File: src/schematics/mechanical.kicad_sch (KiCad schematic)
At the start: 38 parts, among them U1 TPS565242DRDR, U2 TPS562202DRLR, U3 TPS562202DRLR, U4 TPS562202DRLR, U5 LM3880MF*-1AA

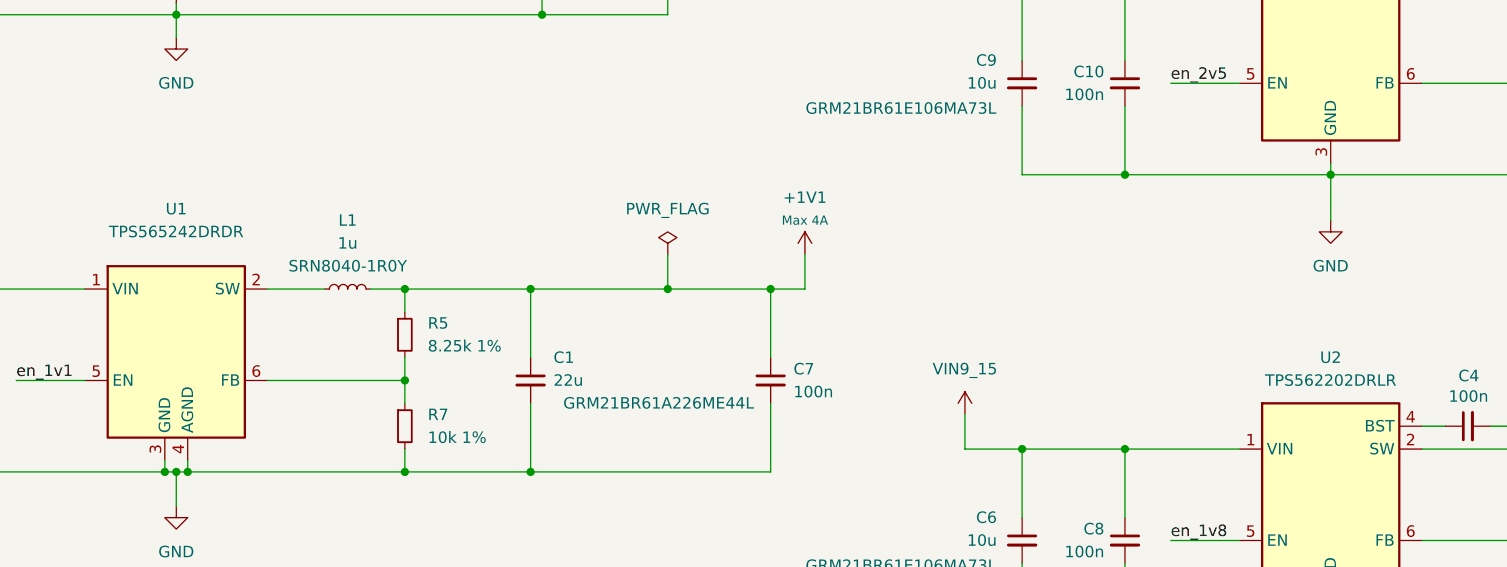
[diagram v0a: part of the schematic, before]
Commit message: Add length matching for DDR on L4 and L6. Todo L1 and redo L6
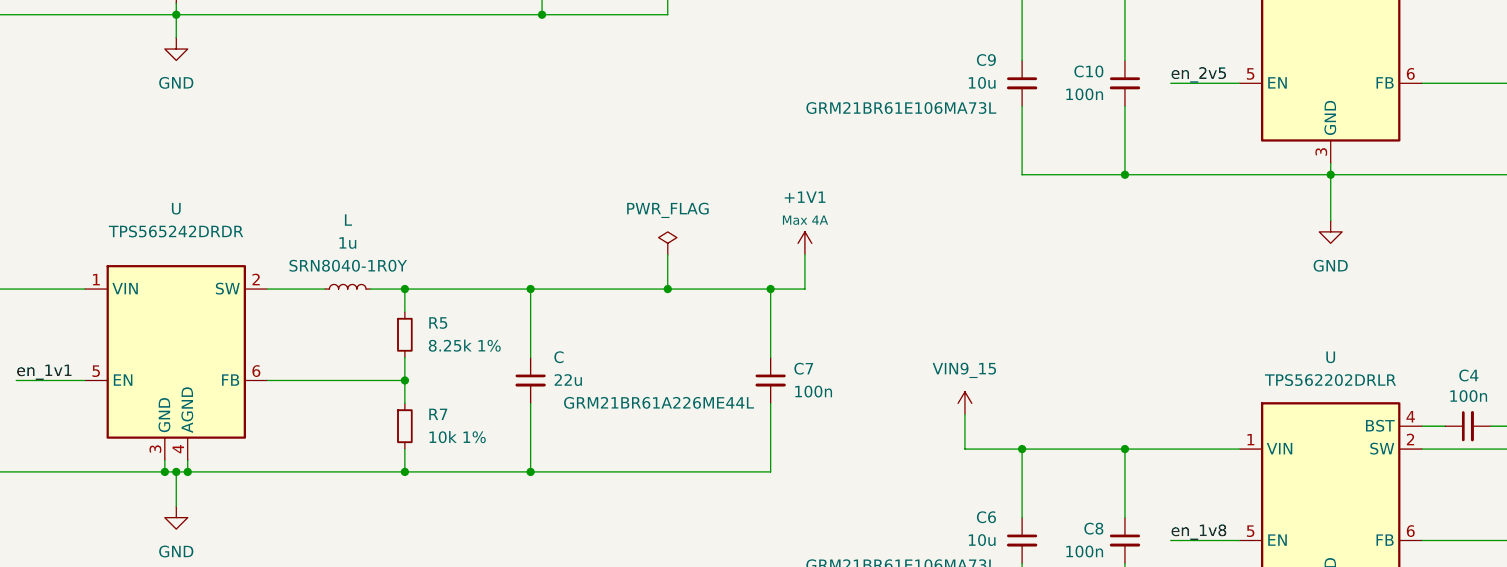
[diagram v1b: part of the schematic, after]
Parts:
- renumbered C1 to C, L1 to L, U2 to U, U1 to U

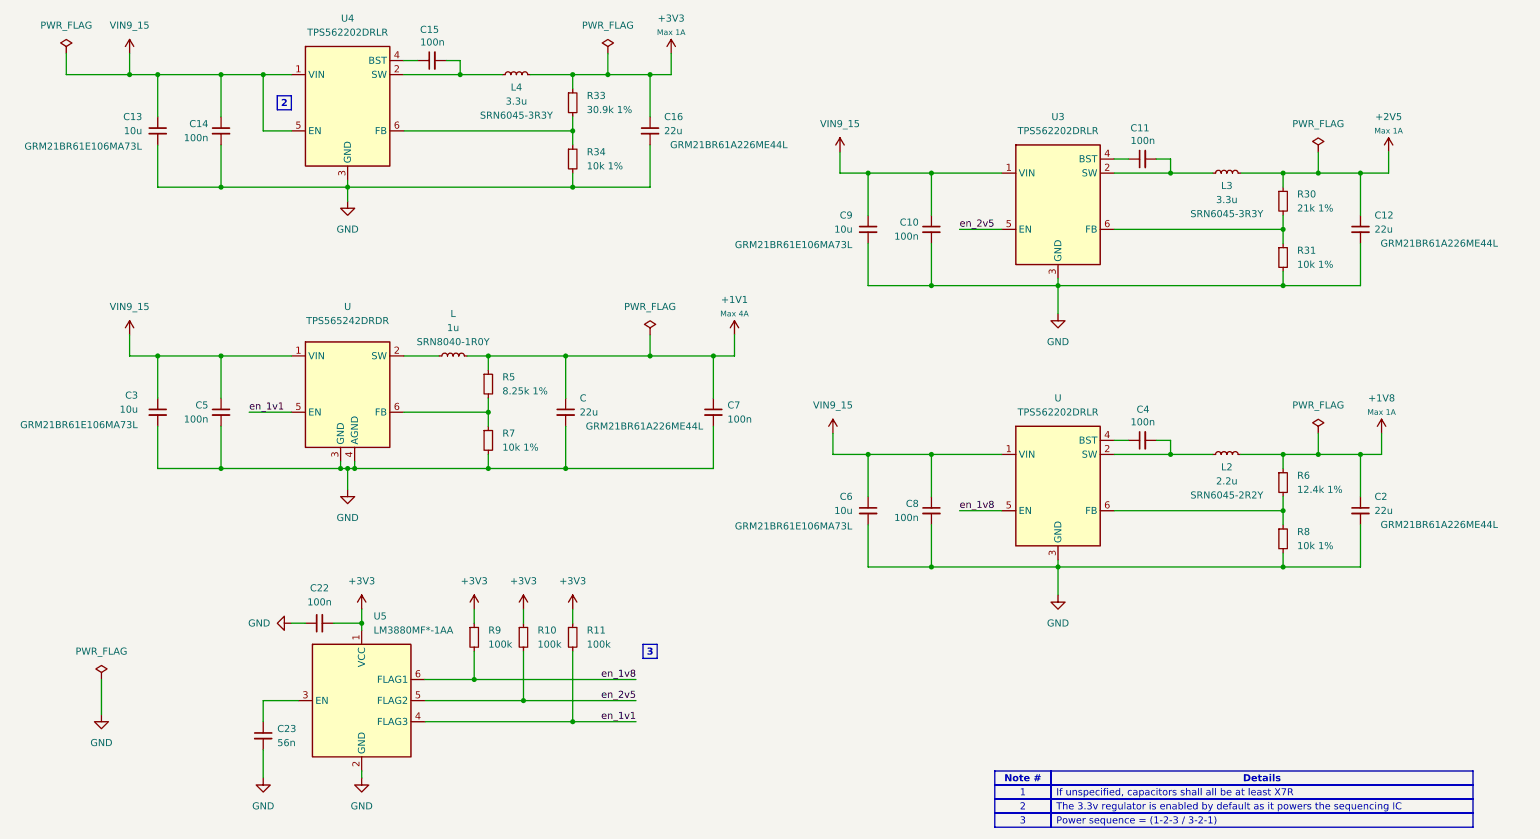
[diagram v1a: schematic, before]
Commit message: Fixed mechanical holes
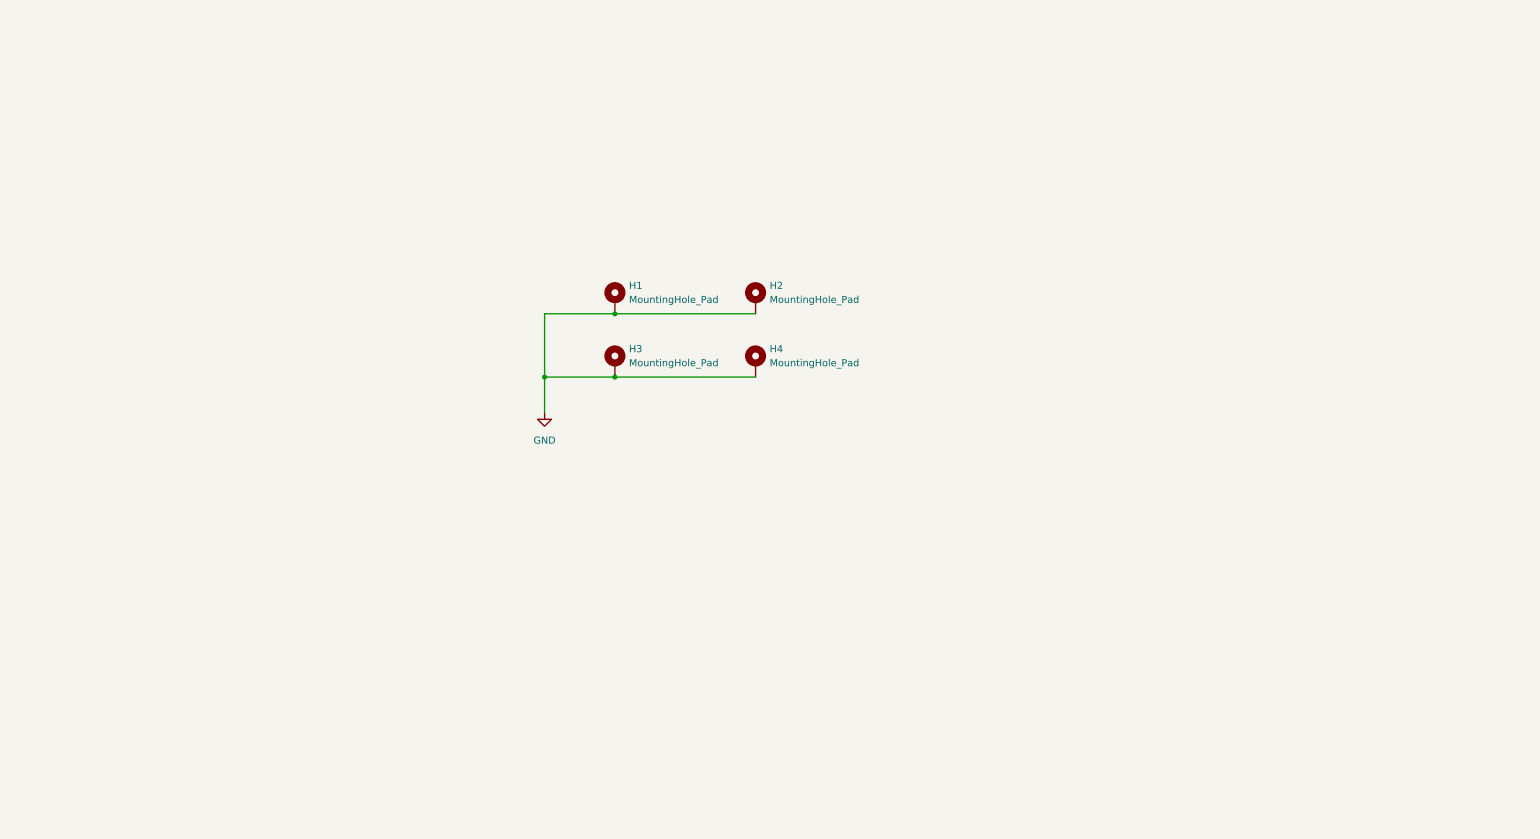
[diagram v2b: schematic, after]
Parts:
- removed C, C12, C16, C2: 22u, Capacitor_SMD:C_0805_2012Metric, symbol Device:C_Small
- removed C10, C14, C5, C7, C8: 100n, Capacitor_SMD:C_0603_1608Metric, symbol Device:C_Small
- removed C11, C15, C22, C4: 100n, Capacitor_SMD:C_0402_1005Metric, symbol Device:C_Small
- removed C13, C3, C6, C9: 10u, Capacitor_SMD:C_0805_2012Metric, symbol Device:C_Small
- removed C23: 56n, Capacitor_SMD:C_0402_1005Metric, symbol Device:C_Small
- removed L: 1u, ECAP5-DPROC:Coilcraft_XAL4020, symbol Device:L_Small
- removed L2: 2.2u, ECAP5-DPROC:Coilcraft_XAL4020, symbol Device:L_Small
- removed L3, L4: 3.3u, ECAP5-DPROC:Coilcraft_XAL4030, symbol Device:L_Small
- removed R10, R11, R9: 100k, Resistor_SMD:R_0402_1005Metric, symbol Device:R_Small
- removed R30: 21k 1%, Resistor_SMD:R_0402_1005Metric, symbol Device:R_Small
- removed R31, R34, R7, R8: 10k 1%, Resistor_SMD:R_0402_1005Metric, symbol Device:R_Small
- removed R33: 30.9k 1%, Resistor_SMD:R_0402_1005Metric, symbol Device:R_Small
- removed R5: 8.25k 1%, Resistor_SMD:R_0402_1005Metric, symbol Device:R_Small
- removed R6: 12.4k 1%, Resistor_SMD:R_0402_1005Metric, symbol Device:R_Small
- removed U, U3, U4: TPS562202DRLR, ECAP5-DPROC:TI_DRL0006A, symbol ECAP5-BSOM:TPS562202DRLR
- removed U: TPS565242DRDR, ECAP5-DPROC:TI_DRL0006A, symbol ECAP5-BSOM:TPS565242DRDR
- removed U5: LM3880MF*-1AA, ECAP5-DPROC:LM3880, symbol ECAP5-BSOM:LM3880
- added H1, H2, H3, H4: MountingHole_Pad, MountingHole:MountingHole_2.2mm_M2_DIN965_Pad_TopBottom, symbol Mechanical:MountingHole_Pad
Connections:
- net GND: now also H1.1, H2.1, H3.1, H4.1
